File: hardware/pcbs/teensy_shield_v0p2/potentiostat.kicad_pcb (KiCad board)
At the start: 2 copper layers, 144.8 x 88.9 mm, 99 parts, among them K1 CONN_3, P1 CONN_2, P10 CONN_2, P11 CONN_2, P12 CONN_2, P13 CONN_5X2, P14 CONN_5X2, P15 CONN_2X2, P16 CONN_2X2, P17 CONN_2, P18 CONN_2, P19 CONN_2, P2 CONN_2, P20 CONN_2, P21 CONN_2, P3 CONN_2, P4 CONN_2, P5 CONN_2, P6 CONN_2, P7 CONN_2, P8 CONN_2, P9 CONN_2, U1 ZXRE060, U10 OPA227, U11 OP07, U12 LT1995, U13 ADG44X, U2 TEENSY3.1, U3 MAX6176AASA+, U4 LT1995, U5 AD8250, U6 MEA1D05XXSC, U7 OPA129, U8 OPA129, U9 ADG44X

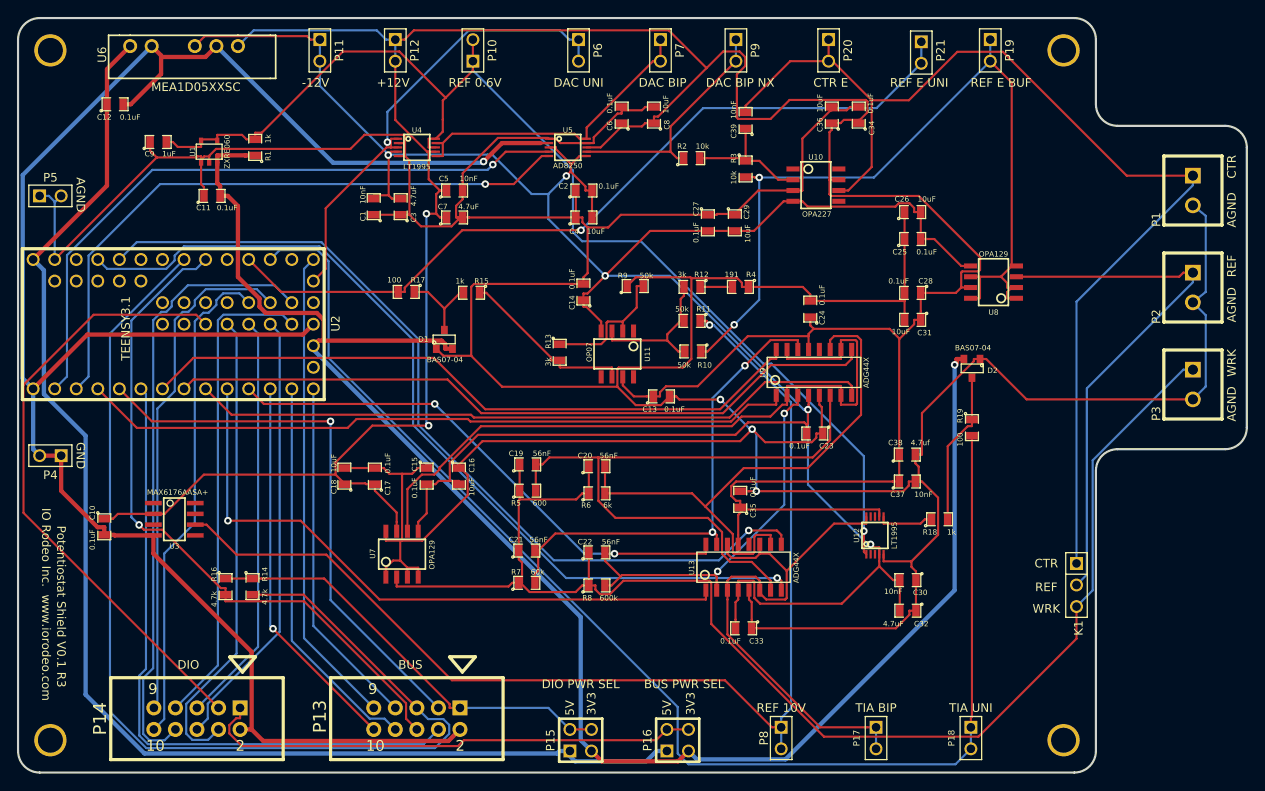
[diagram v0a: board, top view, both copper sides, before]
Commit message: Worked on teensy shield version 0.2. Ported footprints from .mod to .kicad_mod.   Finished initial footprint assignments.
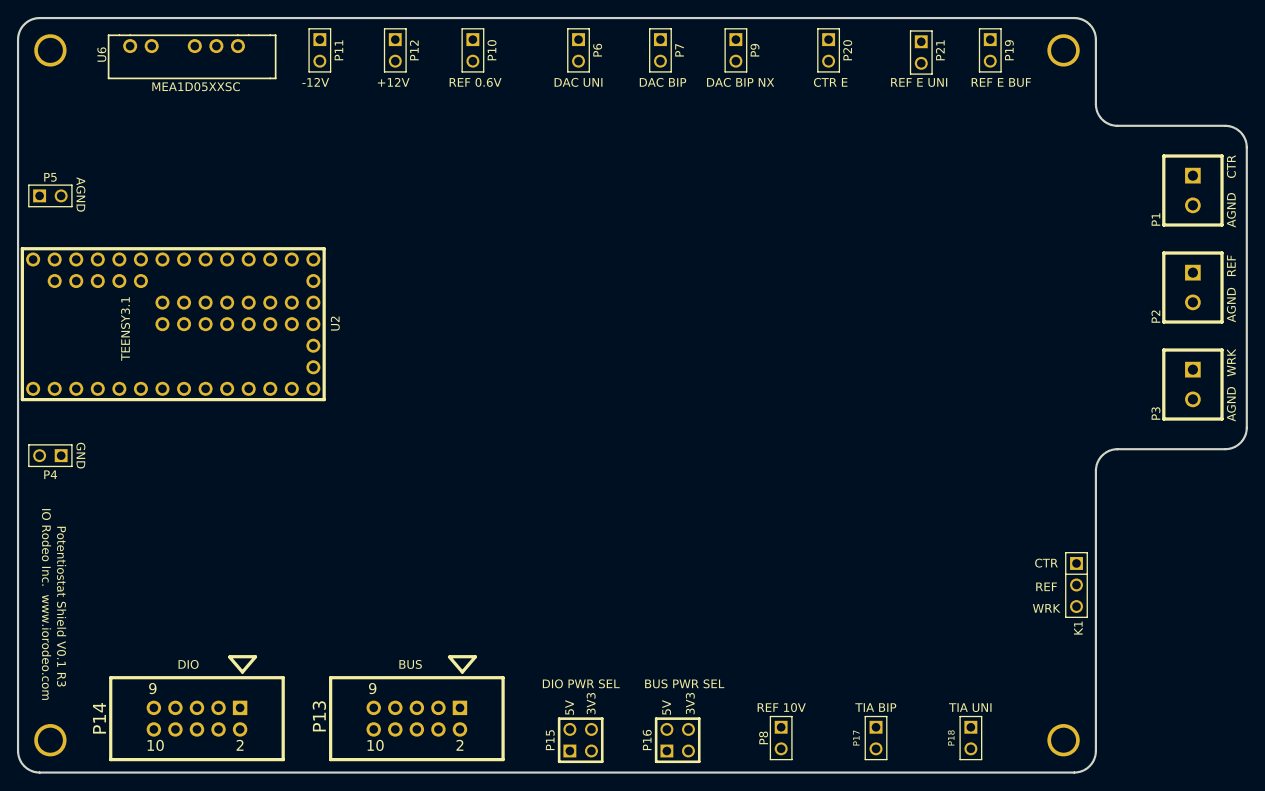
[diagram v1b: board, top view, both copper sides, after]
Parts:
- removed C1, C30, C37, C39, C5: 10nF, SM0805
- removed C10, C11, C12, C13, C14, C15, C17, C2, C23, C24, C25, C27, C28, C33, C34, C35, C6: 0.1uF, SM0805
- removed C16, C18, C26, C29, C31, C36, C4, C8: 10uF, SM0805
- removed C19, C20, C21, C22: 56nF, SM0805
- removed C3, C32, C7: 4.7uF, SM0805
- removed C38: 4.7uf, SM0805
- removed C9: 1uF, SM0805
- removed D1, D2: BAS07-04, SOT23
- removed R1, R15, R18: 1k, SM0805
- removed R10, R11, R9: 50k, SM0805
- removed R12, R13: 3k, SM0805
- removed R14, R16: 4.7k, SM0805
- removed R17, R19: 100, SM0805
- removed R2, R3: 10k, SM0805
- removed R4: 191, SM0805
- removed R5: 600, SM0805
- removed R6: 6k, SM0805
- removed R7: 60k, SM0805
- removed R8: 600k, SM0805
- removed U1: ZXRE060, SOT23-5
- removed U10: OPA227, 8-SOIC-0154
- removed U11: OP07, 8-SOIC-0154
- removed U12, U4: LT1995, MSOP10-0.5
- removed U13, U9: ADG44X, 16-SOIC-0154
- removed U3: MAX6176AASA+, MAXIM-S8
- removed U5: AD8250, MSOP10-0.5
- removed U7, U8: OPA129, 8-SOIC-0154
- K1: footprint PIN_ARRAY_3X1 -> pin_array:PIN_ARRAY_3X1
- P1, P2, P3: footprint CONNBLOCK2 -> ost_connblocks:CONNBLOCK2
- P10, P11, P12, P17, P18, P19, P20, P21, P4, P5, P6, P7, P8, P9: footprint PIN_ARRAY_2X1 -> pin_array:PIN_ARRAY_2X1
- P13, P14: footprint 5X2_SHRD_HEADER -> 5x2_shrd_header:5X2_SHRD_HEADER
- P15, P16: footprint PIN_ARRAY_2X2 -> pin_array:PIN_ARRAY_2X2
- U2: footprint TEENSY3X -> teensy3x:TEENSY3X
- turned P10 to 270 degrees
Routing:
- net /AGND: track 564.3 -> 0.00 mm, vias 3 -> 0
- net /+12V: track 373.5 -> 0.00 mm, vias 2 -> 0
- net /-12V: track 301.1 -> 0.00 mm, vias 5 -> 0
- net /GND: track 229.1 -> 0.00 mm, vias 1 -> 0
- net /3V3: track 194.9 -> 0.00 mm, vias 1 -> 0
- net /WRK_ELECT: track 166.7 -> 0.00 mm
- net /5V: track 156.8 -> 0.00 mm
- net /TIA_OUT_UNI: track 155.7 -> 0.00 mm
- net /REF_0V6: track 140.1 -> 0.00 mm, vias 1 -> 0
- net /REF_10V: track 135.0 -> 0.00 mm, vias 1 -> 0
- net /CTR_ELECT: track 132.8 -> 0.00 mm
- net /SCL: track 129.9 -> 0.00 mm
- net /TIA_SW2_IN4: track 105.7 -> 0.00 mm, vias 1 -> 0
- net /TIA_SW2_IN3: track 103.1 -> 0.00 mm, vias 1 -> 0
- net /REF_ELECT_BUF: track 100.9 -> 0.00 mm, vias 2 -> 0
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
